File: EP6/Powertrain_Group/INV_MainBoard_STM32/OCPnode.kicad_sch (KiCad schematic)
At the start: 7 parts, among them U13 LM393

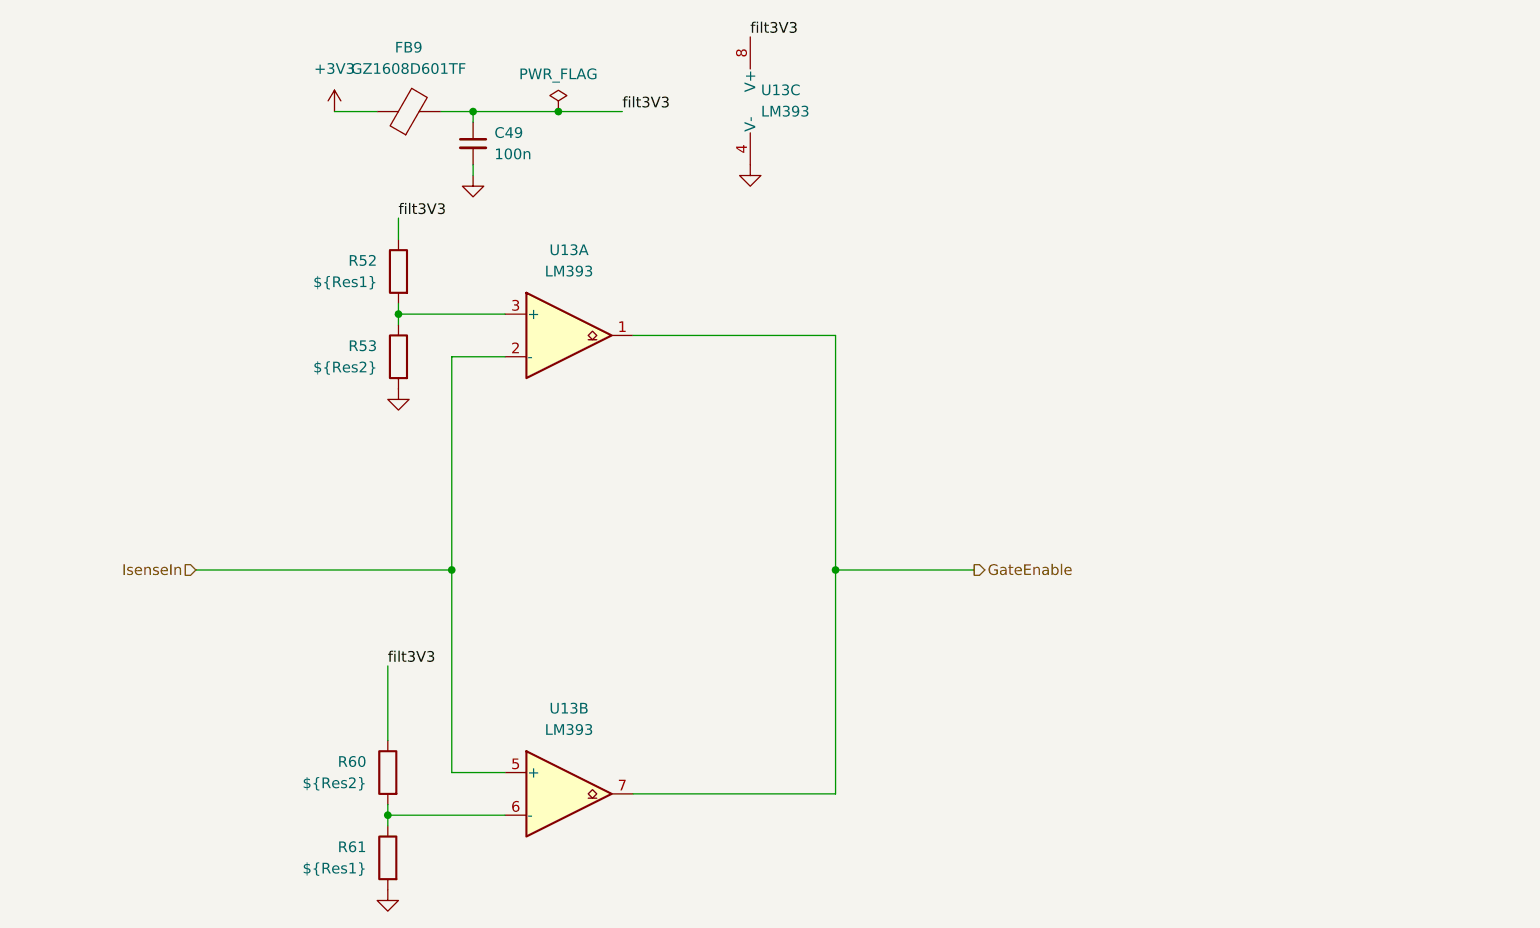
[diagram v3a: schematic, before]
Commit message: update INV_MainBoard_STM32 to V3.0
PCB: INV_MainBoard_STM32 V3.0
V3.0 remove low volte trig
     add RC filt for OCP, OTP
     dedicated OTP, OCP pull down gate enable
     pending: fault hardware OTP/OCP latch
     pending: add QSPI DRAM
     use JST PH
     exterinal pull up for flt, ready
     fix CAN1, 2 label on board
     use 1k, 2k for encoder divider
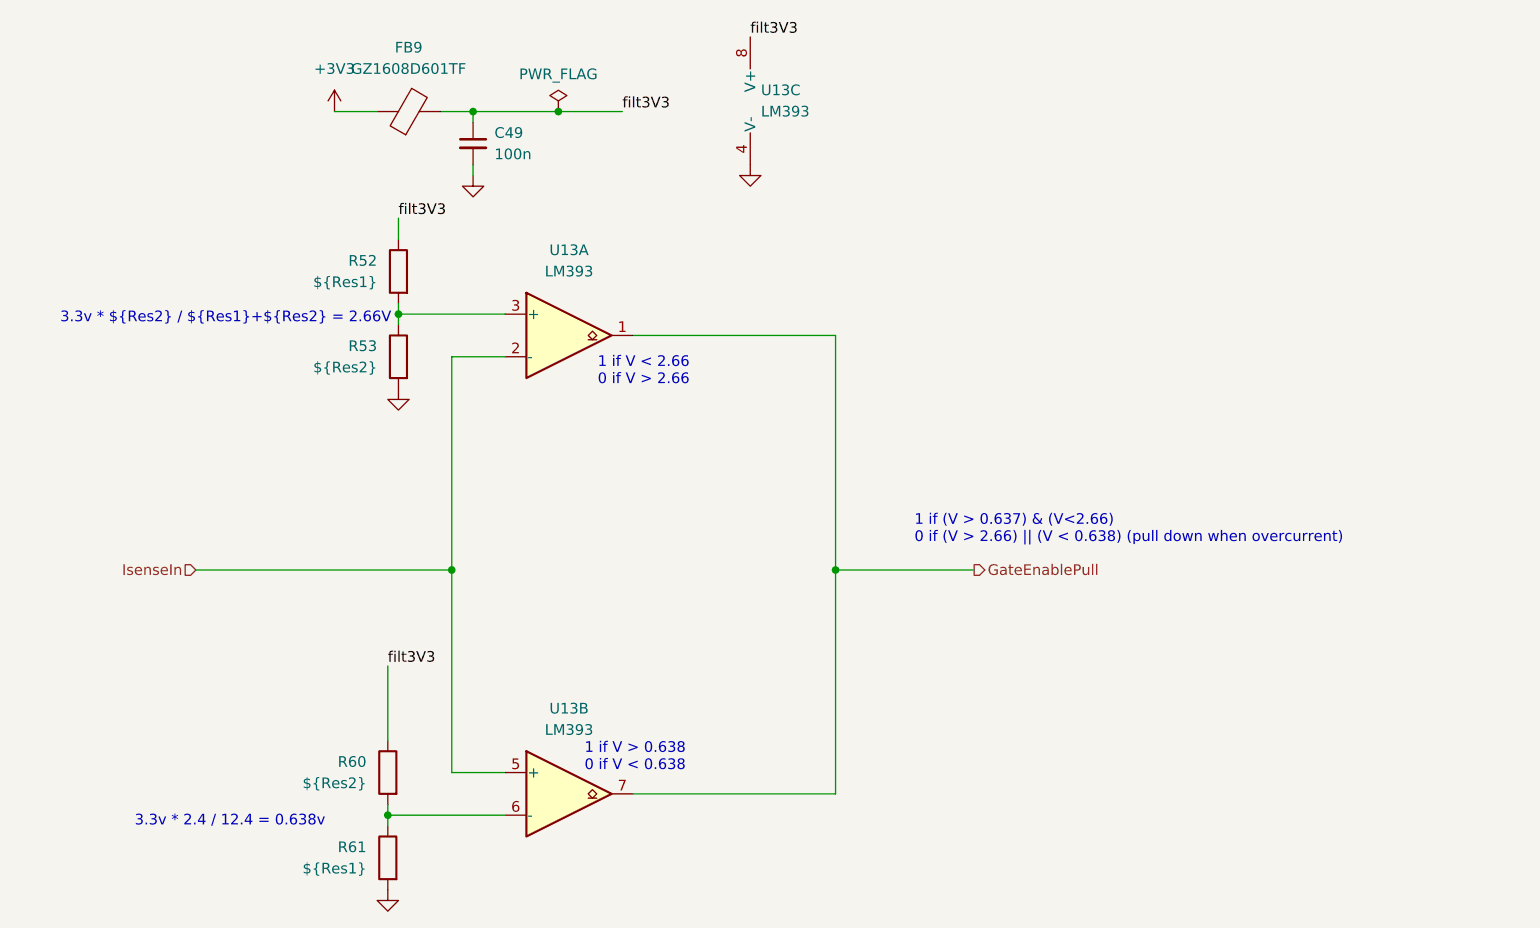
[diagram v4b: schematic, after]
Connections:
- net GateEnable renamed GateEnablePull
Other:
- note added: "1 if (V > 0.637) & (V<2.66) 0 if (V > 2.66) || (V < 0.638) (pull down when overcurrent)"
- note added: "1 if V < 2.66 0 if V > 2.66"
- note added: "1 if V > 0.638 0 if V < 0.638"
- note added: "3.3v * ${Res2} / ${Res1}+${Res2} = 2.66V"
- note added: "3.3v * 2.4 / 12.4 = 0.638v"
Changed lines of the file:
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@@
 	(title_block
 		(title "INV_MainBoard_STM32")
-		(date "2025-02-28")
-		(rev "2.1")
+		(date "2025-06-29")
+		(rev "3.0")
 		(company "NTURacing Team")
 		(comment 1 "郭哲明 Jack Kuo")
@@
 			(width 0)
 			(type default)
+		)
+	)
+	(text "1 if V < 2.66\n0 if V > 2.66"
+		(exclude_from_sim no)
+		(at 133.35 75.438 0)
+		(effects
+			(font
+				(size 1.27 1.27)
+			)
+		)
+	)
+	(text "1 if (V > 0.637) & (V<2.66)\n0 if (V > 2.66) || (V < 0.638) (pull down when overcurrent)"
+		(exclude_from_sim no)
+		(at 165.608 96.012 0)
+		(effects
+			(font
+				(size 1.27 1.27)
+			)
+			(justify left bottom)
+		)
+	)
+	(text "3.3v * ${Res2} / ${Res1}+${Res2} = 2.66V"
+		(exclude_from_sim no)
+		(at 83.566 69.088 0)
+		(effects
+			(font
+				(size 1.27 1.27)
+			)
+		)
+	)
+	(text "3.3v * 2.4 / 12.4 = 0.638v\n"
+		(exclude_from_sim no)
+		(at 84.074 129.032 0)
+		(effects
+			(font
+				(size 1.27 1.27)
+			)
+		)
+	)
+	(text "1 if V > 0.638\n0 if V < 0.638"
+		(exclude_from_sim no)
+		(at 132.334 121.412 0)
+		(effects
+			(font
+				(size 1.27 1.27)
+			)
 		)
 	)
@@
 		)
 	)
-	(hierarchical_label "GateEnable"
+	(hierarchical_label "GateEnablePull"
 		(shape output)
 		(at 172.72 99.06 0)
@@
 					(unit 1)
 				)
-				(path "/963ad98e-e494-4953-a7e0-8b20a365a35d/a8cbfb17-6eb3-4a23-8b1d-6aae5b32a7fb/ceaa5b7a-21ef-4490-9d0f-66aa661daa3d"
-					(reference "#PWR0128")
-					(unit 1)
-				)
 				(path "/963ad98e-e494-4953-a7e0-8b20a365a35d/a8cbfb17-6eb3-4a23-8b1d-6aae5b32a7fb/ebd095ab-b364-4f92-88fd-2a6c5803cc4a"
 					(reference "#PWR0124")
@@
 					(unit 1)
 				)
-				(path "/963ad98e-e494-4953-a7e0-8b20a365a35d/a8cbfb17-6eb3-4a23-8b1d-6aae5b32a7fb/ceaa5b7a-21ef-4490-9d0f-66aa661daa3d"
-					(reference "#PWR0129")
-					(unit 1)
-				)
 				(path "/963ad98e-e494-4953-a7e0-8b20a365a35d/a8cbfb17-6eb3-4a23-8b1d-6aae5b32a7fb/ebd095ab-b364-4f92-88fd-2a6c5803cc4a"
 					(reference "#PWR0125")
@@
 				(path "/963ad98e-e494-4953-a7e0-8b20a365a35d/a8cbfb17-6eb3-4a23-8b1d-6aae5b32a7fb/c1723ad8-cc3f-4769-a58d-f7c6ef8f3681"
 					(reference "R56")
-					(unit 1)
-				)
-				(path "/963ad98e-e494-4953-a7e0-8b20a365a35d/a8cbfb17-6eb3-4a23-8b1d-6aae5b32a7fb/ceaa5b7a-21ef-4490-9d0f-66aa661daa3d"
-					(reference "R54")
 					(unit 1)
 				)
@@
 					(unit 1)
 				)
-				(path "/963ad98e-e494-4953-a7e0-8b20a365a35d/a8cbfb17-6eb3-4a23-8b1d-6aae5b32a7fb/ceaa5b7a-21ef-4490-9d0f-66aa661daa3d"
-					(reference "FB1")
-					(unit 1)
-				)
 				(path "/963ad98e-e494-4953-a7e0-8b20a365a35d/a8cbfb17-6eb3-4a23-8b1d-6aae5b32a7fb/ebd095ab-b364-4f92-88fd-2a6c5803cc4a"
 					(reference "FB8")
@@
 					(unit 1)
 				)
-				(path "/963ad98e-e494-4953-a7e0-8b20a365a35d/a8cbfb17-6eb3-4a23-8b1d-6aae5b32a7fb/ceaa5b7a-21ef-4490-9d0f-66aa661daa3d"
-					(reference "R30")
-					(unit 1)
-				)
 				(path "/963ad98e-e494-4953-a7e0-8b20a365a35d/a8cbfb17-6eb3-4a23-8b1d-6aae5b32a7fb/ebd095ab-b364-4f92-88fd-2a6c5803cc4a"
 					(reference "R51")
@@
 				(path "/963ad98e-e494-4953-a7e0-8b20a365a35d/a8cbfb17-6eb3-4a23-8b1d-6aae5b32a7fb/c1723ad8-cc3f-4769-a58d-f7c6ef8f3681"
 					(reference "R31")
-					(unit 1)
-				)
-				(path "/963ad98e-e494-4953-a7e0-8b20a365a35d/a8cbfb17-6eb3-4a23-8b1d-6aae5b32a7fb/ceaa5b7a-21ef-4490-9d0f-66aa661daa3d"
-					(reference "R29")
 					(unit 1)
 				)
@@
 					(unit 1)
 				)
-				(path "/963ad98e-e494-4953-a7e0-8b20a365a35d/a8cbfb17-6eb3-4a23-8b1d-6aae5b32a7fb/ceaa5b7a-21ef-4490-9d0f-66aa661daa3d"
-					(reference "#PWR099")
-					(unit 1)
-				)
 				(path "/963ad98e-e494-4953-a7e0-8b20a365a35d/a8cbfb17-6eb3-4a23-8b1d-6aae5b32a7fb/ebd095ab-b364-4f92-88fd-2a6c5803cc4a"
 					(reference "#PWR0115")
@@
 				(path "/963ad98e-e494-4953-a7e0-8b20a365a35d/a8cbfb17-6eb3-4a23-8b1d-6aae5b32a7fb/c1723ad8-cc3f-4769-a58d-f7c6ef8f3681"
 					(reference "C47")
-					(unit 1)
-				)
-				(path "/963ad98e-e494-4953-a7e0-8b20a365a35d/a8cbfb17-6eb3-4a23-8b1d-6aae5b32a7fb/ceaa5b7a-21ef-4490-9d0f-66aa661daa3d"
-					(reference "C46")
 					(unit 1)
 				)
@@
 					(unit 3)
 				)
-				(path "/963ad98e-e494-4953-a7e0-8b20a365a35d/a8cbfb17-6eb3-4a23-8b1d-6aae5b32a7fb/ceaa5b7a-21ef-4490-9d0f-66aa661daa3d"
-					(reference "U10")
-					(unit 3)
-				)
 				(path "/963ad98e-e494-4953-a7e0-8b20a365a35d/a8cbfb17-6eb3-4a23-8b1d-6aae5b32a7fb/ebd095ab-b364-4f92-88fd-2a6c5803cc4a"
 					(reference "U12")
@@
 				(path "/963ad98e-e494-4953-a7e0-8b20a365a35d/a8cbfb17-6eb3-4a23-8b1d-6aae5b32a7fb/c1723ad8-cc3f-4769-a58d-f7c6ef8f3681"
 					(reference "R57")
-					(unit 1)
-				)
-				(path "/963ad98e-e494-4953-a7e0-8b20a365a35d/a8cbfb17-6eb3-4a23-8b1d-6aae5b32a7fb/ceaa5b7a-21ef-4490-9d0f-66aa661daa3d"
-					(reference "R55")
 					(unit 1)
 				)
@@
 					(unit 1)
 				)
-				(path "/963ad98e-e494-4953-a7e0-8b20a365a35d/a8cbfb17-6eb3-4a23-8b1d-6aae5b32a7fb/ceaa5b7a-21ef-4490-9d0f-66aa661daa3d"
-					(reference "U10")
-					(unit 1)
-				)
 				(path "/963ad98e-e494-4953-a7e0-8b20a365a35d/a8cbfb17-6eb3-4a23-8b1d-6aae5b32a7fb/ebd095ab-b364-4f92-88fd-2a6c5803cc4a"
 					(reference "U12")
@@
 					(unit 1)
 				)
-				(path "/963ad98e-e494-4953-a7e0-8b20a365a35d/a8cbfb17-6eb3-4a23-8b1d-6aae5b32a7fb/ceaa5b7a-21ef-4490-9d0f-66aa661daa3d"
-					(reference "#PWR081")
-					(unit 1)
-				)
 				(path "/963ad98e-e494-4953-a7e0-8b20a365a35d/a8cbfb17-6eb3-4a23-8b1d-6aae5b32a7fb/ebd095ab-b364-4f92-88fd-2a6c5803cc4a"
 					(reference "#PWR091")
@@
 					(unit 1)
 				)
-				(path "/963ad98e-e494-4953-a7e0-8b20a365a35d/a8cbfb17-6eb3-4a23-8b1d-6aae5b32a7fb/ceaa5b7a-21ef-4490-9d0f-66aa661daa3d"
-					(reference "#PWR0134")
-					(unit 1)
-				)
 				(path "/963ad98e-e494-4953-a7e0-8b20a365a35d/a8cbfb17-6eb3-4a23-8b1d-6aae5b32a7fb/ebd095ab-b364-4f92-88fd-2a6c5803cc4a"
 					(reference "#PWR0126")
@@
 					(unit 2)
 				)
-				(path "/963ad98e-e494-4953-a7e0-8b20a365a35d/a8cbfb17-6eb3-4a23-8b1d-6aae5b32a7fb/ceaa5b7a-21ef-4490-9d0f-66aa661daa3d"
-					(reference "U10")
-					(unit 2)
-				)
 				(path "/963ad98e-e494-4953-a7e0-8b20a365a35d/a8cbfb17-6eb3-4a23-8b1d-6aae5b32a7fb/ebd095ab-b364-4f92-88fd-2a6c5803cc4a"
 					(reference "U12")
@@
 					(unit 1)
 				)
-				(path "/963ad98e-e494-4953-a7e0-8b20a365a35d/a8cbfb17-6eb3-4a23-8b1d-6aae5b32a7fb/ceaa5b7a-21ef-4490-9d0f-66aa661daa3d"
-					(reference "#FLG015")
-					(unit 1)
-				)

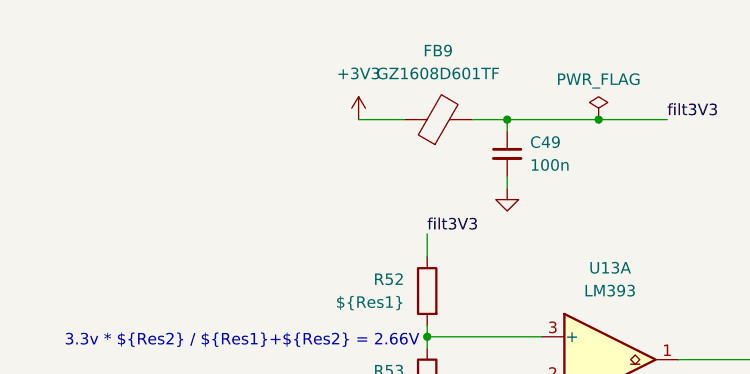
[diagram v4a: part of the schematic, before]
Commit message: update INV_MainBoard_STM32 to V3.1
V3.1 fix R93 to 100R
     add led for OCP, OTP flt
     add default Res for OTP threshold
     add gnd pins for testing
     fix latch circuit
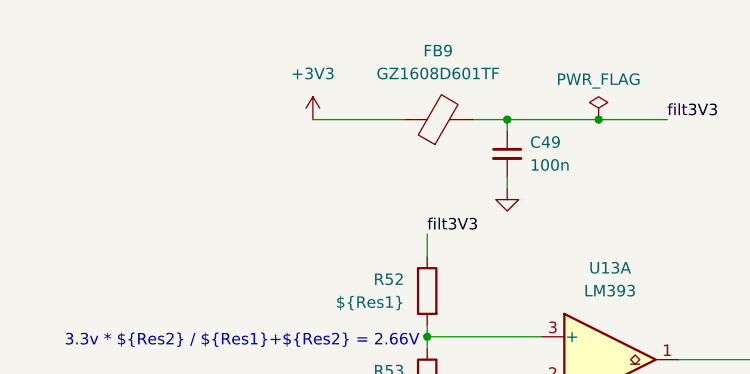
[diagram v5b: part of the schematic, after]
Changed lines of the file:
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@@
 	(title_block
 		(title "INV_MainBoard_STM32")
-		(date "2025-06-29")
-		(rev "3.0")
+		(date "2025-06-30")
+		(rev "3.1")
 		(company "NTURacing Team")
 		(comment 1 "郭哲明 Jack Kuo")
@@
 	(wire
 		(pts
-			(xy 96.52 44.45) (xy 101.6 44.45)
+			(xy 91.44 44.45) (xy 101.6 44.45)
 		)
 		(stroke
@@
 	(symbol
 		(lib_id "power:+3V3")
-		(at 96.52 44.45 0)
+		(at 91.44 44.45 0)
 		(unit 1)
 		(exclude_from_sim no)
@@
 		(fields_autoplaced yes)
 		(property "Reference" "#PWR0118"
-			(at 96.52 48.26 0)
+			(at 91.44 48.26 0)
 			(effects
 				(font
@@
 		)
 		(property "Value" "+3V3"
-			(at 96.52 39.37 0)
+			(at 91.44 39.37 0)
 			(effects
 				(font
@@
 		)
 		(property "Footprint" ""
-			(at 96.52 44.45 0)
+			(at 91.44 44.45 0)
 			(effects
 				(font
@@
 		)
 		(property "Datasheet" ""
-			(at 96.52 44.45 0)
+			(at 91.44 44.45 0)
 			(effects
 				(font
@@
 		)
 		(property "Description" "Power symbol creates a global label with name \"+3V3\""
-			(at 96.52 44.45 0)
-			(effects
-				(font
+			(at 91.44 44.45 0)
+			(effects
+				(font
